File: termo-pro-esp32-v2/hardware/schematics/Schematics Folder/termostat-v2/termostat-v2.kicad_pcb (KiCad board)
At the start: 2 copper layers, 169 x 87 mm, 26 parts, among them J1 Conn_01x08_Pin, Q1 PN2222A, Q2 PN2222A, SW1 SW_Push, SW2 SW_Push, SW3 SW_Push, SW4 SW_Push, U1 NODEMCU-32S, U2 DHT11

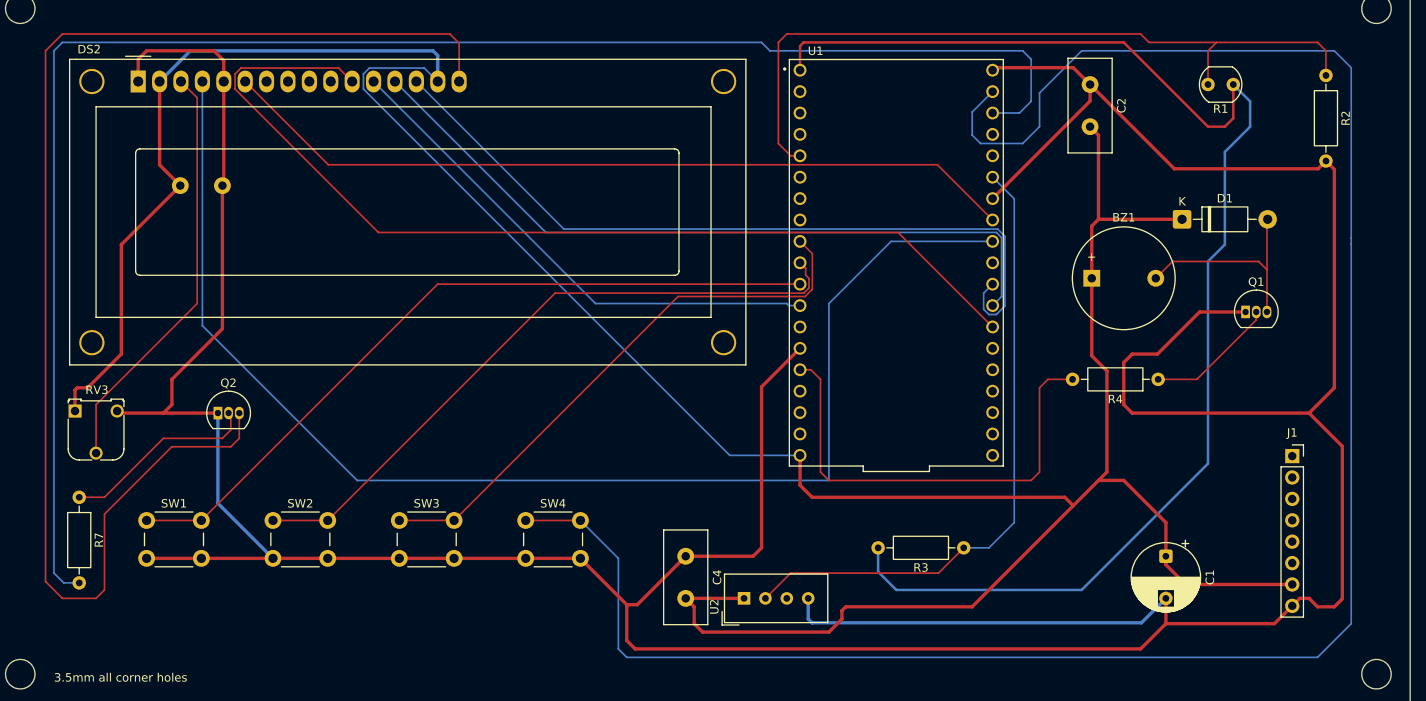
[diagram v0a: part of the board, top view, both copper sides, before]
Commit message: Hardware part of the project is finished.
-DHT11 placement on thermostat unit fixed, pins trace redone.
-USB-C port on thermostat unit placed closer to edge by 4mm.
-Capacitors values recalculated and updated to closest common values, resistors values too.
-Starting unit pcb redone traces as relay and caps have been moved to the back plate.

-Starting & thermostat units PCB are done, inspected.
-Ready for fabrication.
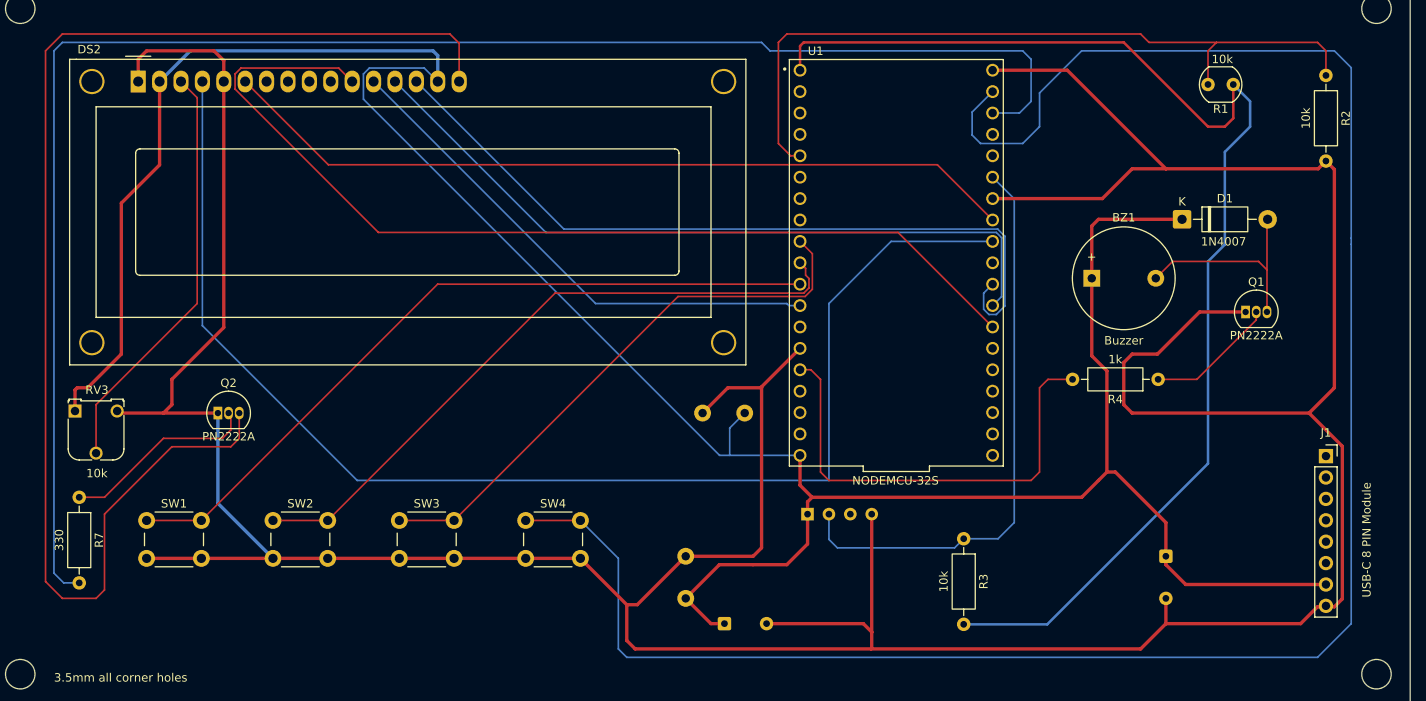
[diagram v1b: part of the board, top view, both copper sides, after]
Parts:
- C1, C2, C4, U2: moved to B.Cu
- C3: value 50V 220nF -> 16V 680uF; footprint Capacitor_THT:C_Disc_D11.0mm_W5.0mm_P5.00mm -> Capacitor_THT:CP_Radial_D8.0mm_P5.00mm
- moved C3 79.1 mm to (159.6, 129.0), turned to 0 degrees
- moved C2 56.6 mm to (162.0, 104.0), turned to 180 degrees
- moved U2 12.5 mm to (169.5, 116.0), turned to -90 degrees
- moved J1 4.00 mm to (231.0, 109.1)
- moved R3 1.08 mm to (188.0, 118.9), turned to -90 degrees
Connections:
- C2 pad 1: GND -> /+VDC
- C2 pad 2: /+VDC -> GND
- C3 pad 1: GND -> /+VDC
- C3 pad 2: /+VDC -> GND
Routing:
- net /+VDC: track 353.9 -> 315.7 mm
- net /V(3.3): track 160.0 -> 147.8 mm
- net Net-(U1-IO21): track 75.3 -> 68.7 mm
- net GND: track 499.4 -> 493.3 mm
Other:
- board text added: "USB-C 8 PIN Module"
